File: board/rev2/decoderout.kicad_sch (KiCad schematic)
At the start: 12 parts, among them U11 IS61LV256AL, U12 74AHCT595

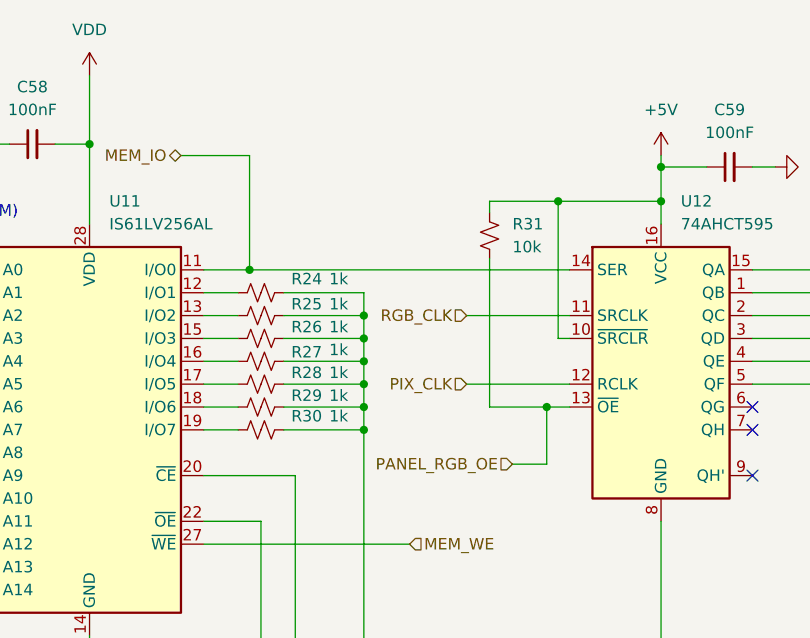
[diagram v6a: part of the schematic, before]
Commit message: Rough full board layout
also, start re-organizing which pins of buffers/gates are used for what

still need to reorder the mem i/o lines to align better

also fix duplicate pullups and fix mem_io isolation res
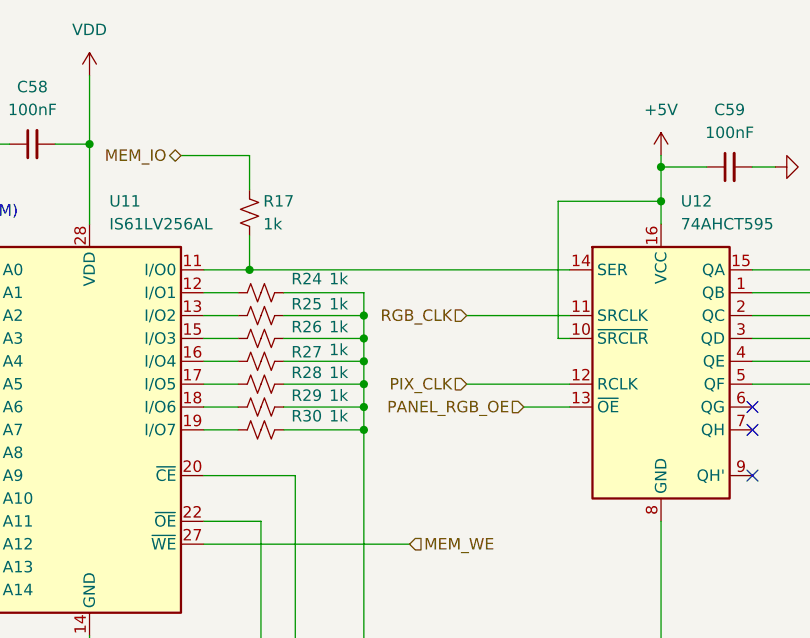
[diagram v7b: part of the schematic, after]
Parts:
- removed R31: 10k, Resistor_SMD:R_0402_1005Metric, symbol Device:R_Small_US
- added R17: 1k, Resistor_SMD:R_0402_1005Metric, symbol Device:R_Small_US
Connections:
- net MEM_IO: now also R17.2; no longer U11.11 (I/O0), U12.14 (SER)
- new net: R17.1, U11.11 (I/O0), U12.14 (SER)
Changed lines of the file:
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@@
-	)
-	(junction
-		(at 172.72 80.01)
-		(diameter 0)
-		(color 0 0 0 0)
 	)
 	(junction
@@
 	)
 	(junction
-		(at 171.45 102.87)
-		(diameter 0)
-		(color 0 0 0 0)
-	)
-	(junction
 		(at 151.13 129.54)
 		(diameter 0)
@@
 	(wire
 		(pts
-			(xy 165.1 86.36) (xy 165.1 102.87)
-		)
-		(stroke
-			(width 0)
-			(type default)
-		)
-	)
-	(wire
-		(pts
 			(xy 139.7 129.54) (xy 120.65 129.54)
 		)
@@
 	(wire
 		(pts
-			(xy 167.64 109.22) (xy 171.45 109.22)
+			(xy 168.91 102.87) (xy 173.99 102.87)
 		)
 		(stroke
@@
 	(wire
 		(pts
-			(xy 138.43 74.93) (xy 138.43 87.63)
+			(xy 138.43 74.93) (xy 138.43 78.74)
 		)
 		(stroke
@@
 	(wire
 		(pts
-			(xy 171.45 109.22) (xy 171.45 102.87)
-		)
-		(stroke
-			(width 0)
-			(type default)
-		)
-	)
-	(wire
-		(pts
 			(xy 143.51 129.54) (xy 139.7 129.54)
 		)
@@
 	(wire
 		(pts
-			(xy 165.1 80.01) (xy 165.1 81.28)
-		)
-		(stroke
-			(width 0)
-			(type default)
-		)
-	)
-	(wire
-		(pts
 			(xy 194.31 87.63) (xy 210.82 87.63)
 		)
@@
 	(wire
 		(pts
+			(xy 138.43 83.82) (xy 138.43 87.63)
+		)
+		(stroke
+			(width 0)
+			(type default)
+		)
+	)
+	(wire
+		(pts
 			(xy 142.24 97.79) (xy 151.13 97.79)
 		)
@@
 	(wire
 		(pts
-			(xy 165.1 80.01) (xy 172.72 80.01)
-		)
-		(stroke
-			(width 0)
-			(type default)
-		)
-	)
-	(wire
-		(pts
 			(xy 151.13 97.79) (xy 151.13 100.33)
 		)
@@
 		)
 	)
-	(wire
-		(pts
-			(xy 171.45 102.87) (xy 173.99 102.87)
-		)
-		(stroke
-			(width 0)
-			(type default)
-		)
-	)
 	(bus
 		(pts
@@
 		(pts
 			(xy 92.71 105.41) (xy 107.95 105.41)
-		)
-		(stroke
-			(width 0)
-			(type default)
-		)
-	)
-	(wire
-		(pts
-			(xy 171.45 102.87) (xy 165.1 102.87)
 		)
 		(stroke
@@
 	(hierarchical_label "PANEL_RGB_OE"
 		(shape input)
-		(at 167.64 109.22 180)
+		(at 168.91 102.87 180)
 		(effects
 			(font
@@
 	(symbol
 		(lib_id "Device:R_Small_US")
+		(at 138.43 81.28 180)
+		(unit 1)
+		(exclude_from_sim no)
+		(in_bom yes)
+		(on_board yes)
+		(dnp no)
+		(property "Reference" "R17"
+			(at 139.954 80.01 0)
+			(effects
+				(font
+					(size 1.27 1.27)
+				)
+				(justify right)
+			)
+		)
+		(property "Value" "1k"
+			(at 139.954 82.55 0)
+			(effects
+				(font
+					(size 1.27 1.27)
+				)
+				(justify right)
+			)
+		)
+		(property "Footprint" "Resistor_SMD:R_0402_1005Metric"
+			(at 138.43 81.28 0)
+			(effects
+				(font
+					(size 1.27 1.27)
+					(color 255 255 194 1)
+				)
+				(hide yes)
+			)
+		)
+		(property "Datasheet" "~"
+			(at 138.43 81.28 0)
+			(effects
+				(font
+					(size 1.27 1.27)
+					(color 255 255 194 1)
+				)
+				(hide yes)
+			)
+		)
+		(property "Description" "Resistor, small US symbol"
+			(at 138.43 81.28 0)
+			(effects
+				(font
+					(size 1.27 1.27)
+					(color 255 255 194 1)
+				)
+				(hide yes)
+			)
+		)
+		(property "Part" "0402WGF1001TCE"
+			(at 138.43 81.28 90)
+			(effects
+				(font
+					(size 1.27 1.27)
+				)
+				(hide yes)
+			)
+		)
+		(property "LCSC" "C11702"
+			(at 138.43 81.28 90)
+			(effects
+				(font
+					(size 1.27 1.27)
+				)
+				(hide yes)
+			)
+		)
+		(pin "2"
+		)
+		(pin "1"
+		)
+		(instances
+			(project "mainboard"
+				(path "/32eb05c7-b4a6-42f3-8fb3-43453631100f/2c9586de-ca2f-4a0b-8ff8-8fdad1d1abcc/1fdb9a92-7450-4af0-9e02-ab97d3a0a007"
+					(reference "R17")
+					(unit 1)
+				)
+				(path "/32eb05c7-b4a6-42f3-8fb3-43453631100f/2c9586de-ca2f-4a0b-8ff8-8fdad1d1abcc/3c07b397-7ce8-476f-8583-4e671a583d8a"
+					(reference "R52")
+					(unit 1)
+				)
+			)
+		)
+	)
+	(symbol
+		(lib_id "Device:R_Small_US")
 		(at 139.7 92.71 90)
 		(unit 1)
@@
 					(unit 1)
 				)
-			)
-		)
-	)
-	(symbol
-		(lib_id "Device:R_Small_US")
-		(at 165.1 83.82 0)
-		(unit 1)
-		(exclude_from_sim no)
-		(in_bom yes)
-		(on_board yes)
-		(dnp no)
-		(property "Reference" "R31"
-			(at 167.64 82.5499 0)
-			(effects
-				(font
-					(size 1.27 1.27)
-				)
-				(justify left)
-			)
-		)
-		(property "Value" "10k"
-			(at 167.64 85.0899 0)
-			(effects
-				(font
-					(size 1.27 1.27)
-				)
-				(justify left)
-			)
-		)
-		(property "Footprint" "Resistor_SMD:R_0402_1005Metric"
-			(at 165.1 83.82 0)
-			(effects
-				(font
-					(size 1.27 1.27)
-					(color 255 255 194 1)
-				)
-				(hide yes)
-			)
-		)
-		(property "Datasheet" "~"
-			(at 165.1 83.82 0)
-			(effects
-				(font
-					(size 1.27 1.27)
-					(color 255 255 194 1)
-				)
-				(hide yes)
-			)
-		)
-		(property "Description" "Resistor, small US symbol"
-			(at 165.1 83.82 0)
-			(effects
-				(font
-					(size 1.27 1.27)
-					(color 255 255 194 1)
-				)
-				(hide yes)
-			)
-		)
-		(property "Part" "0402WGF1002TCE"
-			(at 165.1 83.82 0)
-			(effects
-				(font
-					(size 1.27 1.27)
-				)
-				(hide yes)
-			)
-		)
-		(property "LCSC" "C25744"
-			(at 165.1 83.82 0)
-			(effects
-				(font
-					(size 1.27 1.27)
-				)
-				(hide yes)
-			)
-		)
-		(pin "2"
-		)
-		(pin "1"
-		)
-		(instances
-			(project "mainboard"
-				(path "/32eb05c7-b4a6-42f3-8fb3-43453631100f/2c9586de-ca2f-4a0b-8ff8-8fdad1d1abcc/1fdb9a92-7450-4af0-9e02-ab97d3a0a007"
-					(reference "R31")
-					(unit 1)
-				)
-				(path "/32eb05c7-b4a6-42f3-8fb3-43453631100f/2c9586de-ca2f-4a0b-8ff8-8fdad1d1abcc/3c07b397-7ce8-476f-8583-4e671a583d8a"
-					(reference "R39")
-					(unit 1)
-				)

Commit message: Finish board rev2
woo another pcb
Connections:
- net MEM_A13: now also U11.21 (A10); no longer U11.26 (A13)
- net PIX_CNT_Q0: now also U11.26 (A13); no longer U11.25 (A8)
- net PIX_CNT_Q1: now also U11.25 (A8); no longer U11.24 (A9)
- net PIX_CNT_Q2: now also U11.24 (A9); no longer U11.21 (A10)
